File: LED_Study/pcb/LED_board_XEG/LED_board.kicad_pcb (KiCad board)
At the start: 2 copper layers, 25.4 x 25.4 mm, 4 parts

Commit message: new boards
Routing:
- net /GND: track 15.9 -> 5.33 mm
- net /Vin: track 15.9 -> 5.83 mm
- net Net-(D3-Pad1): track 13.9 -> 4.83 mm
- net Net-(D1-Pad1): track 11.9 -> 4.83 mm
- added copper zone on F.Cu, net /GND
- added copper zone on F.Cu, net /Vin
- added copper zone on F.Cu, net Net-(D1-Pad1)
- added copper zone on F.Cu, net Net-(D3-Pad1)
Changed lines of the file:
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@@
   (gr_circle (center 100 100) (end 112.7 100)
     (stroke (width 0.1) (type default)) (fill none) (layer "Edge.Cuts"))
-  (segment (start 92.955 95.259) (end 95.259 92.955) (width 1) (layer "F.Cu") (net 1))
-  (segment (start 95.259 92.955) (end 98.205 92.955) (width 1) (layer "F.Cu") (net 1))
-  (segment (start 99.57 92.955) (end 98.205 92.955) (width 0.25) (layer "F.Cu") (net 1))
-  (segment (start 92.955 99.57) (end 92.955 98.205) (width 0.25) (layer "F.Cu") (net 1))
-  (segment (start 92.955 98.205) (end 92.955 95.259) (width 1) (layer "F.Cu") (net 1))
-  (segment (start 98.205 108.955) (end 97.25 108) (width 1) (layer "F.Cu") (net 3))
-  (segment (start 92.955 101.795) (end 92.955 107.045) (width 1) (layer "F.Cu") (net 3))
-  (segment (start 92.955 107.045) (end 92 108) (width 1) (layer "F.Cu") (net 3))
-  (segment (start 92.955 100.43) (end 92.955 101.795) (width 0.25) (layer "F.Cu") (net 3))
-  (segment (start 97.25 108) (end 92 108) (width 1) (layer "F.Cu") (net 3))
-  (segment (start 99.57 108.955) (end 98.205 108.955) (width 0.25) (layer "F.Cu") (net 3))
+  (segment (start 99.57 92.955) (end 99.57 93.93) (width 0.25) (layer "F.Cu") (net 1))
+  (segment (start 92.955 98.545) (end 93 98.5) (width 0.25) (layer "F.Cu") (net 1))
+  (segment (start 92.955 99.57) (end 92.955 98.545) (width 0.25) (layer "F.Cu") (net 1))
+  (segment (start 99.57 93.93) (end 99.5 94) (width 0.25) (layer "F.Cu") (net 1))
+  (segment (start 98.045 92.955) (end 98 93) (width 0.25) (layer "F.Cu") (net 1))
+  (segment (start 93.93 99.57) (end 94 99.5) (width 0.25) (layer "F.Cu") (net 1))
+  (segment (start 92.955 99.57) (end 93.93 99.57) (width 0.25) (layer "F.Cu") (net 1))
+  (segment (start 99.57 92.955) (end 98.045 92.955) (width 0.25) (layer "F.Cu") (net 1))
+  (segment (start 99.57 108.955) (end 98.545 108.955) (width 0.25) (layer "F.Cu") (net 3))
+  (segment (start 94.43 100.43) (end 94.5 100.5) (width 0.25) (layer "F.Cu") (net 3))
+  (segment (start 98.545 108.955) (end 98.5 109) (width 0.25) (layer "F.Cu") (net 3))
+  (segment (start 92.955 100.43) (end 94.43 100.43) (width 0.25) (layer "F.Cu") (net 3))
+  (segment (start 92.955 100.43) (end 92.955 102.455) (width 0.25) (layer "F.Cu") (net 3))
+  (segment (start 99.57 108.955) (end 99.57 109.93) (width 0.25) (layer "F.Cu") (net 3))
+  (segment (start 99.57 109.93) (end 99.5 110) (width 0.25) (layer "F.Cu") (net 3))
+  (segment (start 92.955 102.455) (end 93 102.5) (width 0.25) (layer "F.Cu") (net 3))
   (via (at 92 108) (size 3) (drill 1.5) (layers "F.Cu" "B.Cu") (free) (net 3))
-  (segment (start 108 92) (end 102.75 92) (width 1) (layer "F.Cu") (net 4))
-  (segment (start 108 92) (end 108 97.25) (width 1) (layer "F.Cu") (net 4))
-  (segment (start 108.955 98.205) (end 108 97.25) (width 1) (layer "F.Cu") (net 4))
-  (segment (start 101.795 92.955) (end 102.75 92) (width 1) (layer "F.Cu") (net 4))
-  (segment (start 108.955 99.57) (end 108.955 98.205) (width 0.25) (layer "F.Cu") (net 4))
-  (segment (start 100.43 92.955) (end 101.795 92.955) (width 0.25) (layer "F.Cu") (net 4))
+  (segment (start 100.43 92.955) (end 100.43 93.93) (width 0.25) (layer "F.Cu") (net 4))
+  (segment (start 108.955 99.57) (end 110.43 99.57) (width 0.25) (layer "F.Cu") (net 4))
+  (segment (start 108.955 98.545) (end 109 98.5) (width 0.25) (layer "F.Cu") (net 4))
+  (segment (start 100.43 93.93) (end 100.5 94) (width 0.25) (layer "F.Cu") (net 4))
+  (segment (start 100.43 92.955) (end 101.955 92.955) (width 0.25) (layer "F.Cu") (net 4))
+  (segment (start 110.43 99.57) (end 110.5 99.5) (width 0.25) (layer "F.Cu") (net 4))
+  (segment (start 101.955 92.955) (end 102 93) (width 0.25) (layer "F.Cu") (net 4))
+  (segment (start 108.955 99.57) (end 108.955 98.545) (width 0.25) (layer "F.Cu") (net 4))
   (via (at 108 92) (size 3) (drill 1.5) (layers "F.Cu" "B.Cu") (free) (net 4))
-  (segment (start 108.966 103.632) (end 103.643 108.955) (width 1) (layer "F.Cu") (net 6))
-  (segment (start 108.966 102.13) (end 108.966 103.632) (width 1) (layer "F.Cu") (net 6))
-  (segment (start 100.43 108.955) (end 102.119 108.955) (width 0.25) (layer "F.Cu") (net 6))
-  (segment (start 108.955 102.119) (end 108.966 102.13) (width 1) (layer "F.Cu") (net 6))
-  (segment (start 108.955 100.43) (end 108.955 102.119) (width 0.25) (layer "F.Cu") (net 6))
-  (segment (start 103.643 108.955) (end 102.119 108.955) (width 1) (layer "F.Cu") (net 6))
+  (segment (start 100.43 108.955) (end 100.43 109.93) (width 0.25) (layer "F.Cu") (net 6))
+  (segment (start 108.955 101.455) (end 109 101.5) (width 0.25) (layer "F.Cu") (net 6))
+  (segment (start 101.955 108.955) (end 102 109) (width 0.25) (layer "F.Cu") (net 6))
+  (segment (start 109.93 100.43) (end 110 100.5) (width 0.25) (layer "F.Cu") (net 6))
+  (segment (start 100.43 108.955) (end 101.955 108.955) (width 0.25) (layer "F.Cu") (net 6))
+  (segment (start 108.955 100.43) (end 109.93 100.43) (width 0.25) (layer "F.Cu") (net 6))
+  (segment (start 108.955 100.43) (end 108.955 101.455) (width 0.25) (layer "F.Cu") (net 6))
+  (segment (start 100.43 109.93) (end 100.5 110) (width 0.25) (layer "F.Cu") (net 6))
+  (zone (net 1) (net_name "Net-(D1-Pad1)") (layer "F.Cu") (hatch edge 0.5)
+    (priority 3)
+    (connect_pads (clearance 0.5))
+    (min_thickness 0.25) (filled_areas_thickness no)
+    (fill yes (thermal_gap 0.5) (thermal_bridge_width 0.5))
+    (polygon
+      (pts
+        (xy 100 100)
+        (xy 100 87)
+        (xy 87 87)
+        (xy 87 100)
+      )
+    )
+  )
+  (zone (net 4) (net_name "/GND") (layer "F.Cu") (hatch edge 0.5)
+    (connect_pads (clearance 0.5))
+    (min_thickness 0.25) (filled_areas_thickness no)
+    (fill yes (thermal_gap 0.5) (thermal_bridge_width 0.5))
+    (polygon
+      (pts
+        (xy 100 100)
+        (xy 100 87)
+        (xy 113 87)
+        (xy 113 100)
+      )
+    )
+  )
+  (zone (net 3) (net_name "/Vin") (layer "F.Cu") (hatch edge 0.5)
+    (priority 2)
+    (connect_pads (clearance 0.5))
+    (min_thickness 0.25) (filled_areas_thickness no)
+    (fill yes (thermal_gap 0.5) (thermal_bridge_width 0.5))
+    (polygon
+      (pts
+        (xy 100 100)
+        (xy 100 113)
+        (xy 87 113)
+        (xy 87 100)
+      )
+    )
+  )
+  (zone (net 6) (net_name "Net-(D3-Pad1)") (layer "F.Cu") (hatch edge 0.5)
+    (priority 1)
+    (connect_pads (clearance 0.5))
+    (min_thickness 0.25) (filled_areas_thickness no)
+    (fill yes (thermal_gap 0.5) (thermal_bridge_width 0.5))
+    (polygon
+      (pts
+        (xy 100 100)
+        (xy 113 100)
+        (xy 113 113)
+        (xy 100 113)
+      )
+    )
+  )
 )

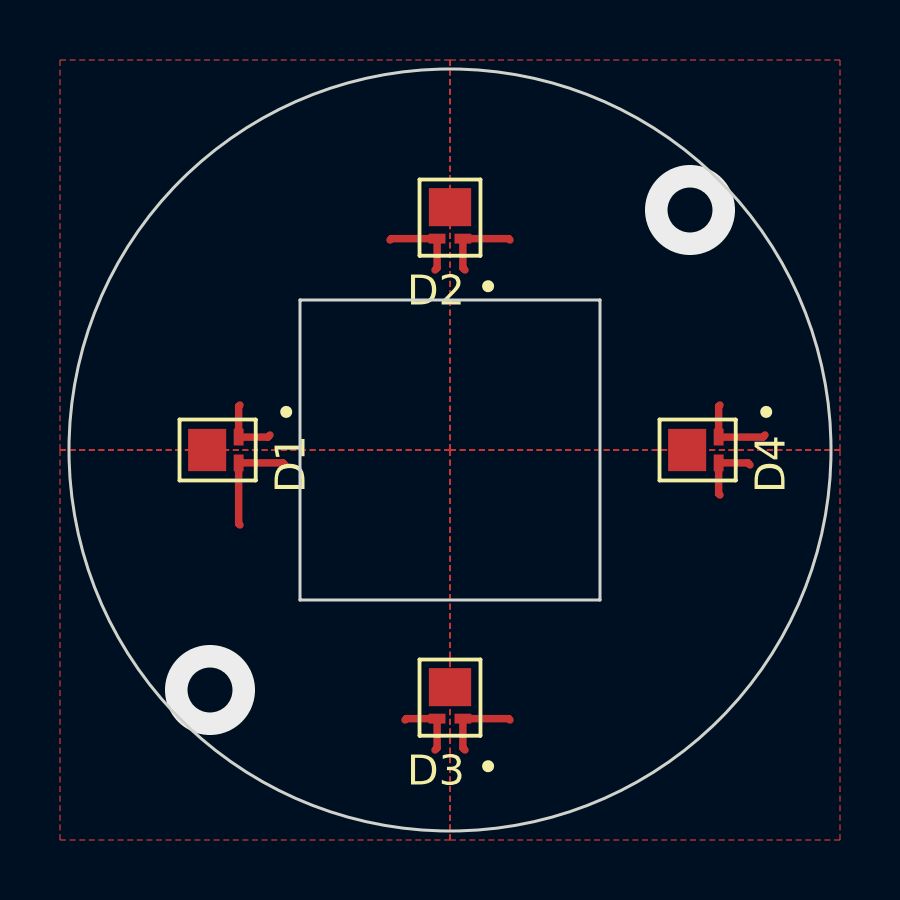
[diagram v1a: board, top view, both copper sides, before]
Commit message: updated boards and ordered from PCBway
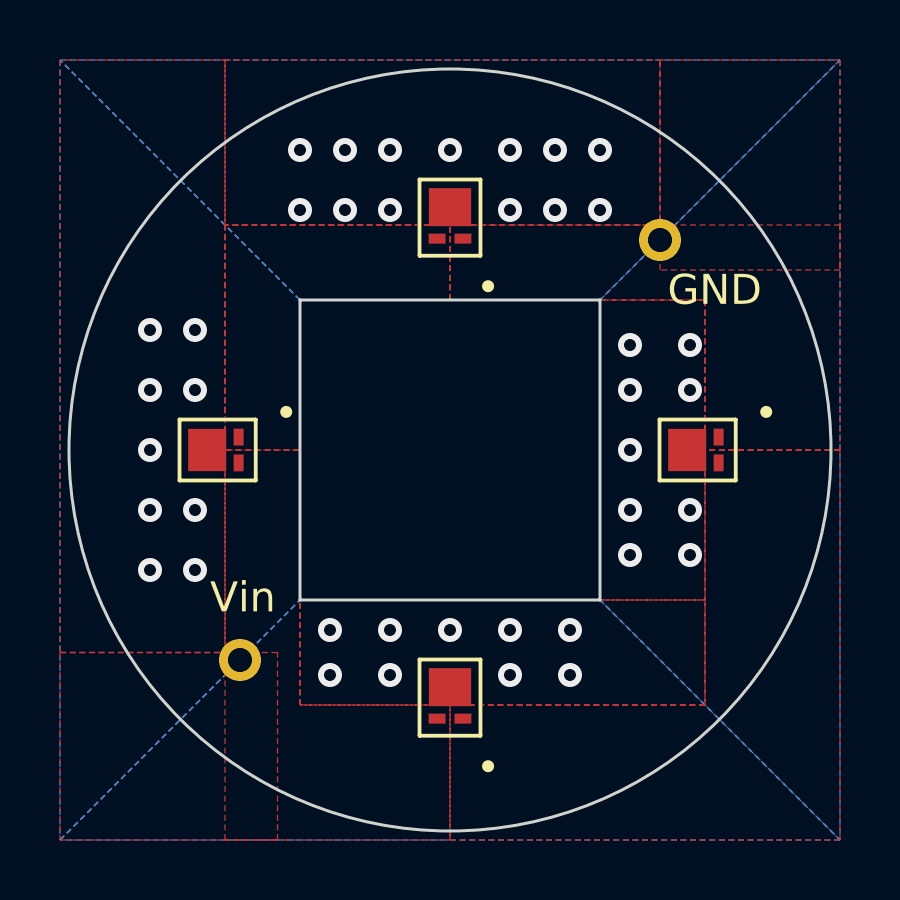
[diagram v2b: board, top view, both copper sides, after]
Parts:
- added J1: Conn_01x01_Pin, Connector_PinHeader_1.00mm:PinHeader_1x01_P1.00mm_Vertical, F.Cu at (93.0, 107.0)
- added J2: Conn_01x01_Pin, Connector_PinHeader_1.00mm:PinHeader_1x01_P1.00mm_Vertical, F.Cu at (107.0, 93.0)
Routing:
- net /Vin: track 5.83 -> 0.00 mm, vias 1 -> 0
- net /GND: track 5.33 -> 0.00 mm, vias 1 -> 0
- net Net-(D3-Pad1): track 4.83 -> 0.00 mm
- net Net-(D1-Pad1): track 4.83 -> 0.00 mm
- net unconnected-(D4-EXP-Pad3): vias 0 -> 9
- net unconnected-(D3-EXP-Pad3): vias 0 -> 9
- net unconnected-(D2-EXP-Pad3): vias 0 -> 13
- net unconnected-(D1-EXP-Pad3): vias 0 -> 9
- added copper zone on B.Cu, net unconnected-(D1-EXP-Pad3)
- added copper zone on F.Cu, net unconnected-(D1-EXP-Pad3)
- added copper zone on B.Cu, net unconnected-(D2-EXP-Pad3)
- added copper zone on F.Cu, net unconnected-(D2-EXP-Pad3)
- added copper zone on B.Cu, net unconnected-(D3-EXP-Pad3)
- added copper zone on F.Cu, net unconnected-(D3-EXP-Pad3)
- added copper zone on B.Cu, net unconnected-(D4-EXP-Pad3)
- added copper zone on F.Cu, net unconnected-(D4-EXP-Pad3)
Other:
- board text added: "GND"
- board text added: "Vin"
